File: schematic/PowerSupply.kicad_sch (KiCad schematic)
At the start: 0 parts

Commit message: Create power supply schematic
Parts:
- added C1, C3: 100nF, symbol Device:C
- added C2, C4: 10uF, symbol Device:C
- added J1: TYPE-C-31-M-12, TYPE-C-31-M-12:HRO_TYPE-C-31-M-12, symbol TYPE-C-31-M-12:TYPE-C-31-M-12
- added R1, R2: 5.1k, symbol Device:R
- added U1: AMS1117-3.3, Package_TO_SOT_SMD:SOT-223-3_TabPin2, symbol Regulator_Linear:AMS1117-3.3
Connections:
- new net: J1.B5 (CC2), R1.1
- new net: J1.A5 (CC1), R2.1
- new net: J1.A6 (DP1), J1.B6 (DP2)
- new net: J1.A7 (DN1), J1.B7 (DN2)
- new net +3.3V: C3.1, C4.1, U1.2 (VO)
- new net +5V: C1.1, C2.1, J1.A4_B9 (VBUS), J1.B4_A9 (VBUS), U1.3 (VI)
- new net GND: C1.2, C2.2, C3.2, C4.2, J1.A1_B12 (GND), J1.B1_A12 (GND), J1.S1 (SHIELD), J1.S2 (SHIELD), J1.S3 (SHIELD), J1.S4 (SHIELD), R1.2, R2.2, U1.1 (GND)
- no-connect marks 0 -> 2

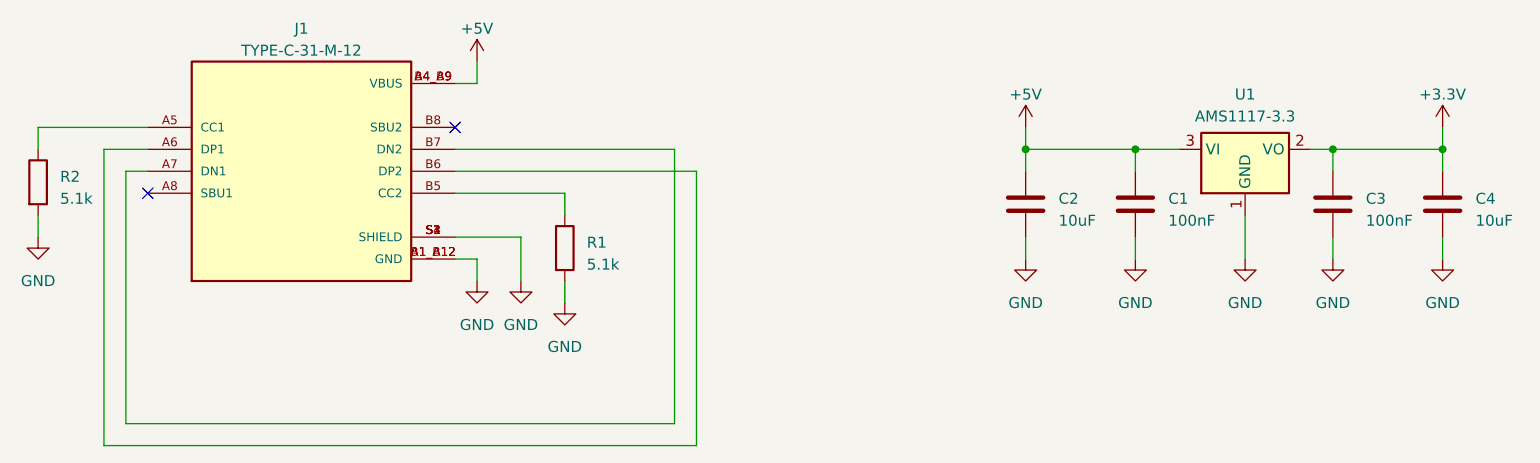
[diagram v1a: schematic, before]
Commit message: Assign footprints
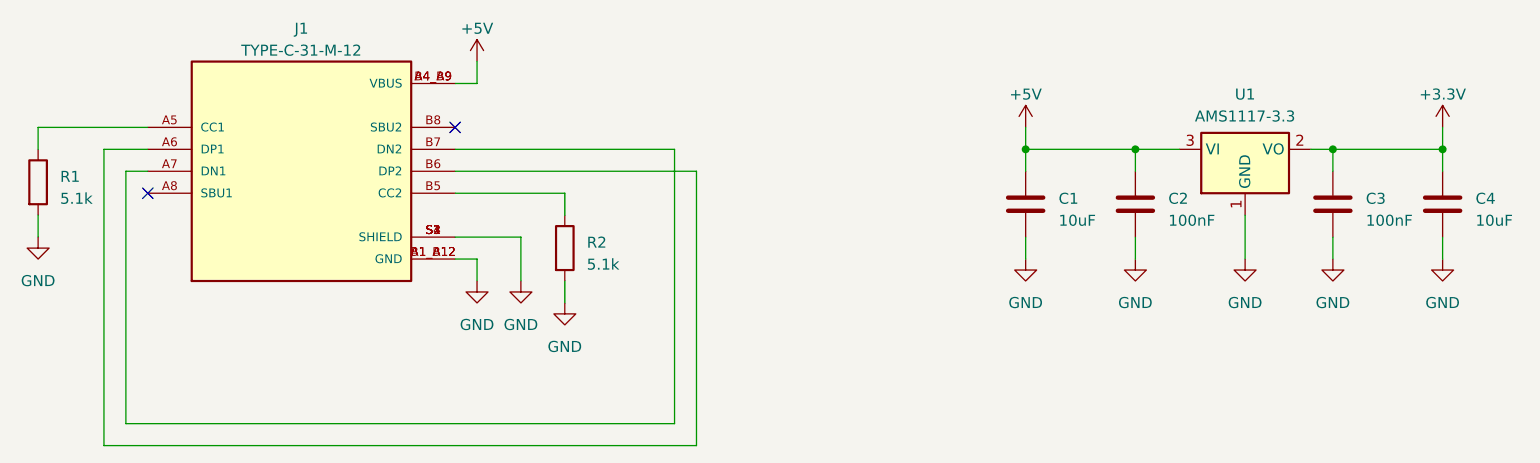
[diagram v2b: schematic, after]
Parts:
- C1: renamed from C2; footprint (none) -> Capacitor_SMD:C_0603_1608Metric
- C2: renamed from C1; footprint (none) -> Capacitor_SMD:C_0603_1608Metric
- C3, C4: footprint (none) -> Capacitor_SMD:C_0603_1608Metric
- R1: renamed from R2; footprint (none) -> Resistor_SMD:R_0603_1608Metric
- R2: renamed from R1; footprint (none) -> Resistor_SMD:R_0603_1608Metric

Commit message: Setup PCB for production
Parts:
- C1, C4: LCSC (none) -> C19702
- C2, C3: LCSC (none) -> C1591
- J1: LCSC (none) -> C165948
- R1, R2: LCSC (none) -> C23186
- U1: LCSC (none) -> C6186
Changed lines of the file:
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@@
+      (effects (font (size 1.27 1.27)) hide)
+    )
+    (property "LCSC" "C1591" (at 190.5 100.33 0)
       (effects (font (size 1.27 1.27)) hide)
     )
@@
       (effects (font (size 1.27 1.27)) hide)
     )
+    (property "LCSC" "C23186" (at 124.46 105.41 0)
+      (effects (font (size 1.27 1.27)) hide)
+    )
     (pin "1")
     (pin "2")
@@
       (effects (font (size 1.27 1.27)) hide)
     )
+    (property "LCSC" "C23186" (at 63.5 97.79 0)
+      (effects (font (size 1.27 1.27)) hide)
+    )
     (pin "1")
     (pin "2")
@@
     )
     (property "Datasheet" "http://www.advanced-monolithic.com/pdf/ds1117.pdf" (at 205.74 100.33 0)
+      (effects (font (size 1.27 1.27)) hide)
+    )
+    (property "LCSC" "C6186" (at 203.2 93.98 0)
       (effects (font (size 1.27 1.27)) hide)
     )
@@
     (property "MANUFACTURER" "HRO Electronics Co., Ltd." (at 93.98 96.52 0)
       (effects (font (size 1.27 1.27)) (justify bottom) hide)
+    )
+    (property "LCSC" "C165948" (at 93.98 96.52 0)
+      (effects (font (size 1.27 1.27)) hide)
     )
     (pin "A1_B12")
@@
       (effects (font (size 1.27 1.27)) hide)
     )
+    (property "LCSC" "C19702" (at 226.06 100.33 0)
+      (effects (font (size 1.27 1.27)) hide)
+    )
     (pin "1")
     (pin "2")
@@
       (effects (font (size 1.27 1.27)) hide)
     )
+    (property "LCSC" "C19702" (at 177.8 100.33 0)
+      (effects (font (size 1.27 1.27)) hide)
+    )
     (pin "1")
     (pin "2")
@@
       (effects (font (size 1.27 1.27)) hide)
     )
+    (property "LCSC" "C1591" (at 213.36 100.33 0)
+      (effects (font (size 1.27 1.27)) hide)
+    )
